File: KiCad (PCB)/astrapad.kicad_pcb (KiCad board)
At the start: 2 copper layers, 106.9 x 53.6 mm, 34 parts, among them J1 OLED_DISPLAY, SW1 SW_Push, SW13 RotaryEncoder_Switch, SW2 SW_Push, SW3 SW_Push, SW5 SW_Push, SW6 SW_Push, SW7 SW_Push, SW8 SW_Push, U1 XIAO-RP2040-DIP

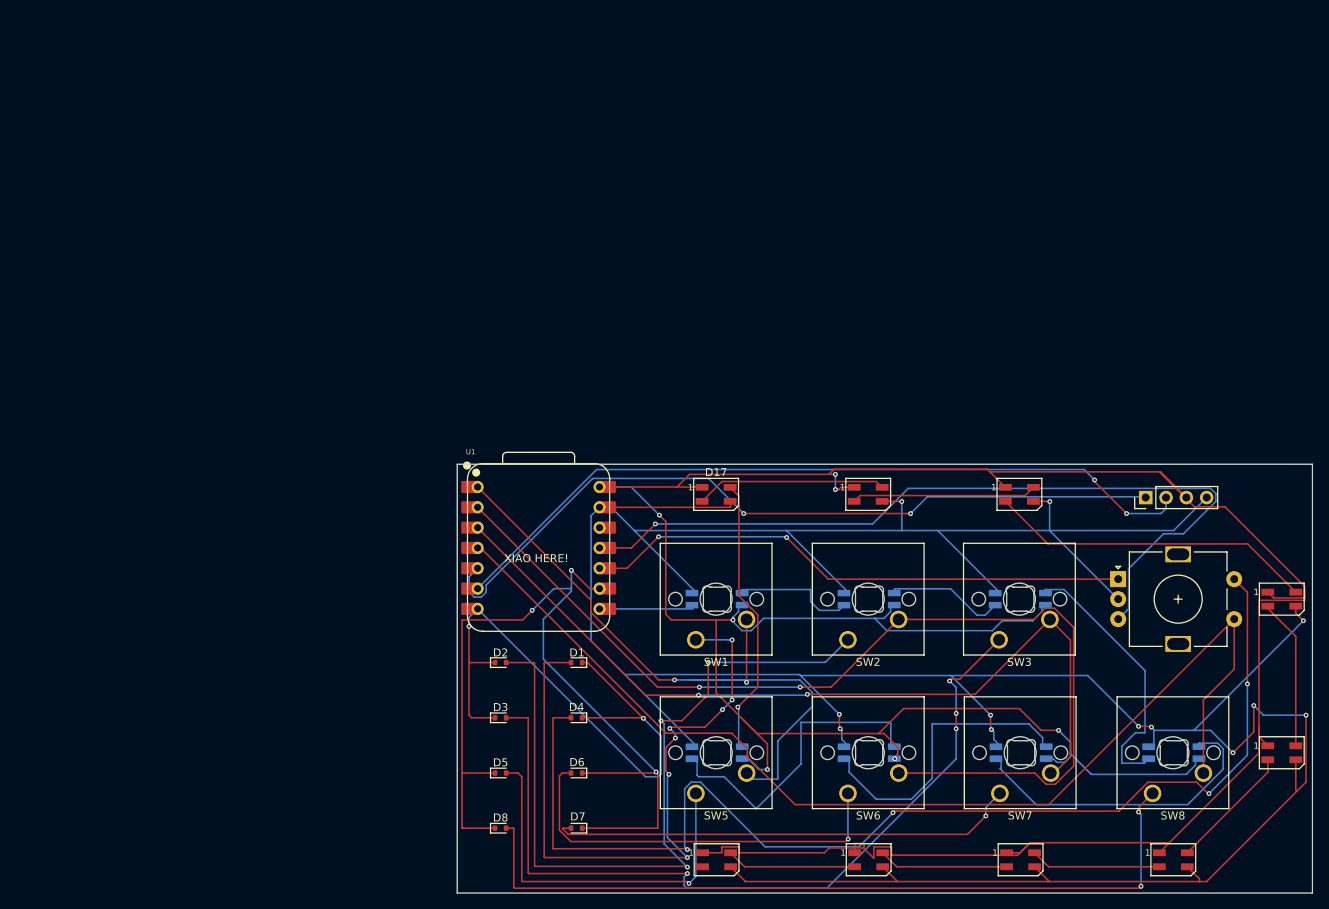
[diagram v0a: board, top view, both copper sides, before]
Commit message: Switching from FreeCAD to Fusion360 Due to the several and constant issues I'm having with FreeCAD, I will be switching to Fusion360 If you wish to know why I was using FreeCAD in the first place, it's because Fusion360 is not available on Linux
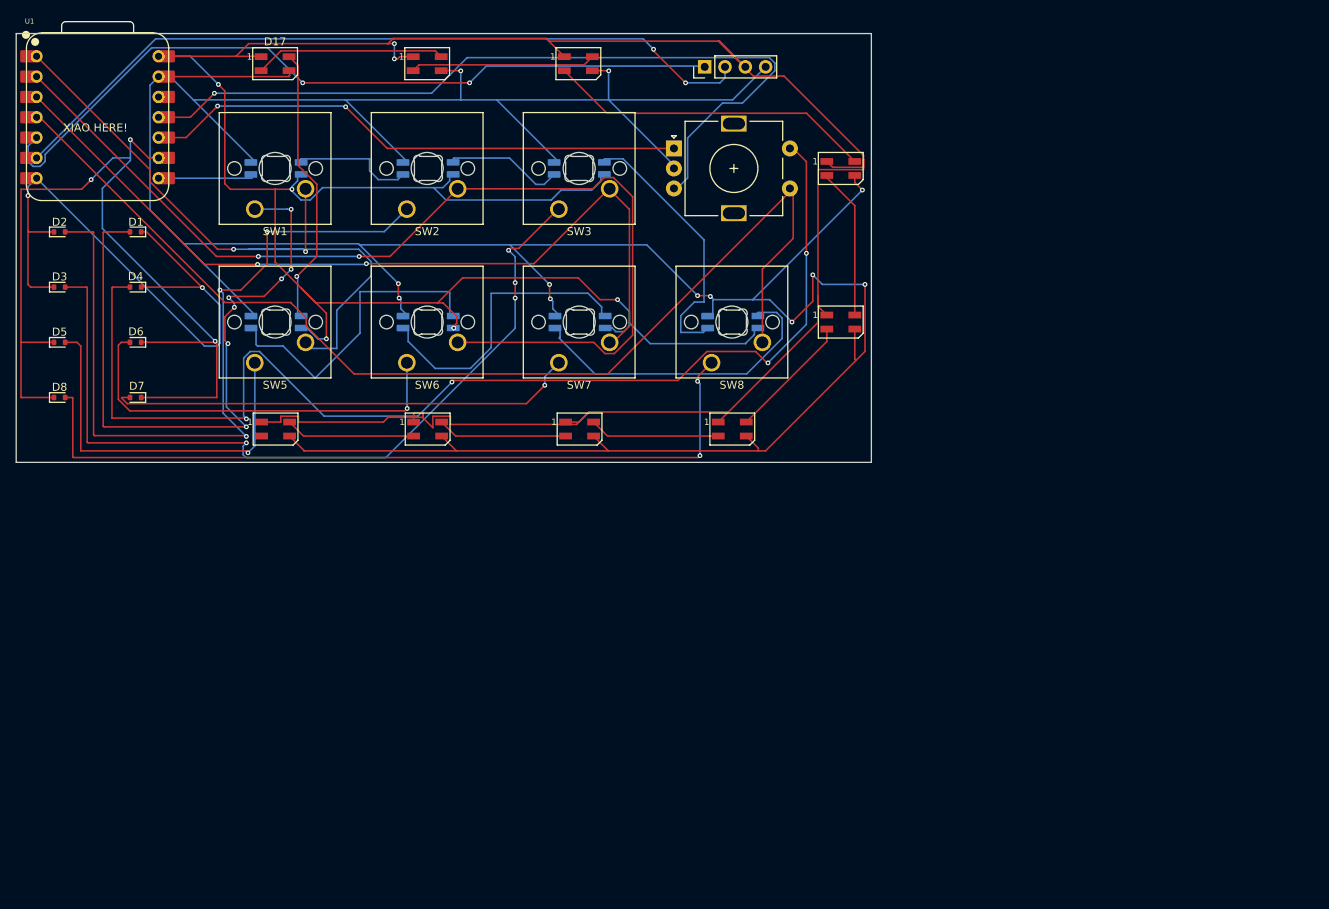
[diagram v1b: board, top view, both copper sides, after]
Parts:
- moved SW13 77.3 mm to (82.2, 14.4)
- moved SW6 77.1 mm to (48.8, 41.1)
- moved SW5 77.1 mm to (29.8, 41.1)
- moved SW8 77.1 mm to (86.9, 41.1)
- moved D1 77.1 mm to (14.9, 24.8)
- moved D10 77.1 mm to (32.5, 16.9)
- moved D11 77.1 mm to (51.5, 16.9)
- moved D12 77.1 mm to (70.4, 16.9)
- moved D13 77.1 mm to (89.6, 36.1)
- moved D14 77.1 mm to (70.5, 36.1)
- moved D15 77.1 mm to (51.5, 36.1)
- moved D16 77.1 mm to (32.5, 36.1)
- moved D17 77.1 mm to (32.4, 3.76)
- moved D18 77.1 mm to (51.4, 3.76)
- moved D19 77.1 mm to (70.3, 3.76)
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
